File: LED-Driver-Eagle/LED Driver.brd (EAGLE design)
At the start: 21.3 x 25.4 mm, 10 parts, among them U3 LM4041A12DBZ

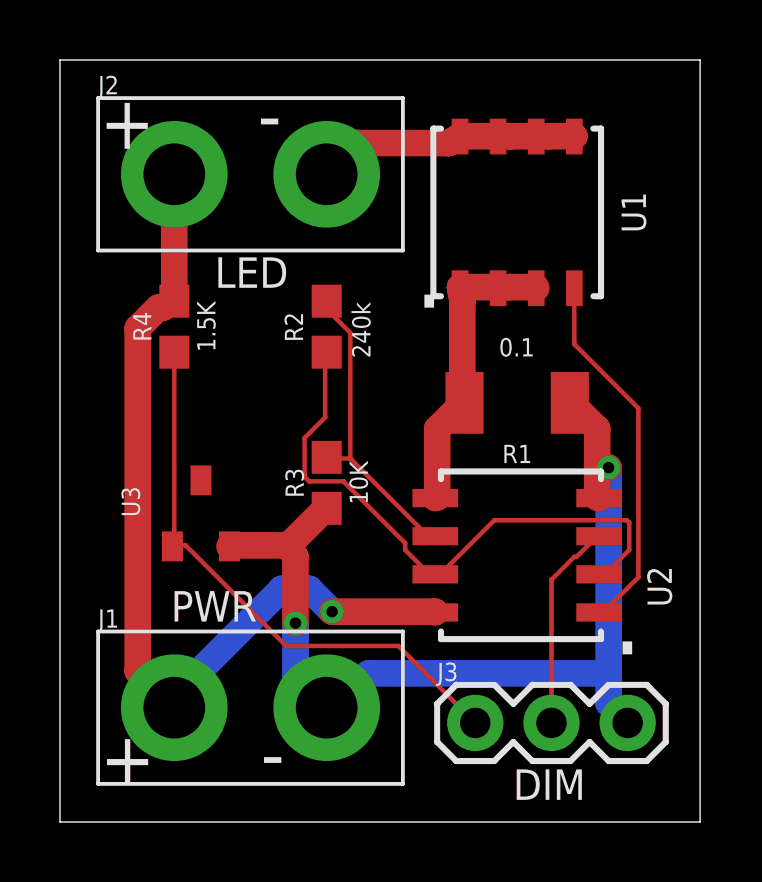
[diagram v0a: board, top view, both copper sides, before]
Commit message: Changed U1 and U2 to MF and OA
Updated Gerbers and eagle board files
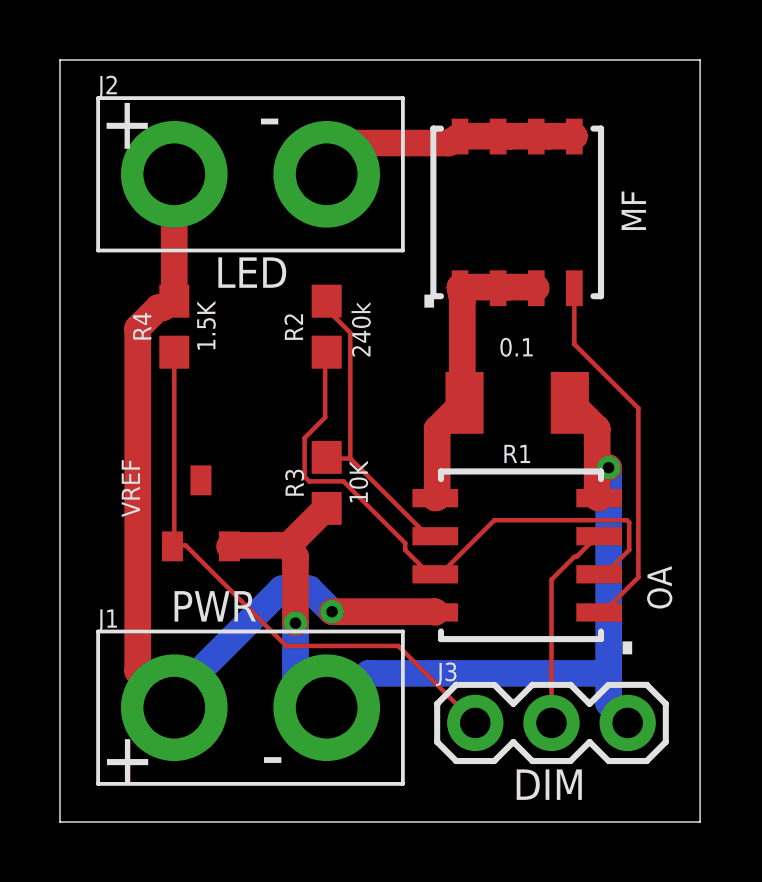
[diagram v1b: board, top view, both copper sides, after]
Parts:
- renumbered U$1 to M$F, U$2 to O$A
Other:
- board text added: "MF"
- board text added: "OA"
- board text added: "VREF"
- board text removed: "U1"
- board text removed: "U2"
- board text removed: "U3"
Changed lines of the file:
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@@
 <drawing>
 <settings>
-<setting alwaysvectorfont="yes"/>
+<setting alwaysvectorfont="no"/>
 <setting verticaltext="up"/>
 </settings>
 <grid distance="0.5" unitdist="mil" unit="mil" style="lines" multiple="1" display="yes" altdistance="5" altunitdist="mil" altunit="mil"/>
 <layers>
-<layer number="1" name="Top" color="4" fill="1" visible="no" active="yes"/>
+<layer number="1" name="Top" color="4" fill="1" visible="yes" active="yes"/>
 <layer number="2" name="Route2" color="1" fill="3" visible="no" active="no"/>
 <layer number="3" name="Route3" color="4" fill="3" visible="no" active="no"/>
@@
 <layer number="19" name="Unrouted" color="6" fill="1" visible="yes" active="yes"/>
 <layer number="20" name="Dimension" color="24" fill="1" visible="yes" active="yes"/>
-<layer number="21" name="tPlace" color="7" fill="1" visible="no" active="yes"/>
+<layer number="21" name="tPlace" color="7" fill="1" visible="yes" active="yes"/>
 <layer number="22" name="bPlace" color="7" fill="1" visible="yes" active="yes"/>
-<layer number="23" name="tOrigins" color="15" fill="1" visible="no" active="yes"/>
+<layer number="23" name="tOrigins" color="15" fill="1" visible="yes" active="yes"/>
 <layer number="24" name="bOrigins" color="15" fill="1" visible="yes" active="yes"/>
-<layer number="25" name="tNames" color="7" fill="1" visible="no" active="yes"/>
+<layer number="25" name="tNames" color="7" fill="1" visible="yes" active="yes"/>
 <layer number="26" name="bNames" color="7" fill="1" visible="yes" active="yes"/>
-<layer number="27" name="tValues" color="7" fill="1" visible="no" active="yes"/>
-<layer number="28" name="bValues" color="7" fill="1" visible="no" active="yes"/>
+<layer number="27" name="tValues" color="7" fill="1" visible="yes" active="yes"/>
+<layer number="28" name="bValues" color="7" fill="1" visible="yes" active="yes"/>
 <layer number="29" name="tStop" color="7" fill="3" visible="no" active="yes"/>
 <layer number="30" name="bStop" color="7" fill="6" visible="no" active="yes"/>
@@
 <layer number="37" name="tTest" color="7" fill="1" visible="no" active="yes"/>
 <layer number="38" name="bTest" color="7" fill="1" visible="no" active="yes"/>
-<layer number="39" name="tKeepout" color="4" fill="11" visible="no" active="yes"/>
+<layer number="39" name="tKeepout" color="4" fill="11" visible="yes" active="yes"/>
 <layer number="40" name="bKeepout" color="1" fill="11" visible="yes" active="yes"/>
-<layer number="41" name="tRestrict" color="4" fill="10" visible="no" active="yes"/>
+<layer number="41" name="tRestrict" color="4" fill="10" visible="yes" active="yes"/>
 <layer number="42" name="bRestrict" color="1" fill="10" visible="yes" active="yes"/>
 <layer number="43" name="vRestrict" color="2" fill="10" visible="no" active="yes"/>
-<layer number="44" name="Drills" color="7" fill="1" visible="no" active="yes"/>
+<layer number="44" name="Drills" color="7" fill="1" visible="yes" active="yes"/>
 <layer number="45" name="Holes" color="7" fill="1" visible="yes" active="yes"/>
 <layer number="46" name="Milling" color="3" fill="1" visible="no" active="yes"/>
@@
 <layer number="49" name="Reference" color="7" fill="1" visible="no" active="yes"/>
 <layer number="50" name="dxf" color="7" fill="1" visible="no" active="no"/>
-<layer number="51" name="tDocu" color="7" fill="1" visible="no" active="yes"/>
+<layer number="51" name="tDocu" color="7" fill="1" visible="yes" active="yes"/>
 <layer number="52" name="bDocu" color="7" fill="1" visible="yes" active="yes"/>
 <layer number="53" name="tGND_GNDA" color="7" fill="9" visible="no" active="no"/>
@@
 </layers>
 <board>
-<fusionsync huburn="a.cGVyc29uYWw6dWUyYjA2ZTQw" projecturn="a.cGVyc29uYWw6dWUyYjA2ZTQwIzIwMTgwMjIzMTE5NDc3OTU2" f3durn="urn:adsk.wipprod:dm.lineage:CXPcsSRXTwSbw_zEyj-MFA" pcbguid="f8d63bc8-81ed-4c37-9df4-4ae1279349d0" lastpulledtime="" lastsyncedchangeguid="bf620849-5e47-bcb0-3e1e-9827651a09dc"/>
+<fusionsync huburn="a.cGVyc29uYWw6dWUyYjA2ZTQw" projecturn="a.cGVyc29uYWw6dWUyYjA2ZTQwIzIwMTgwMjIzMTE5NDc3OTU2" f3durn="urn:adsk.wipprod:dm.lineage:CXPcsSRXTwSbw_zEyj-MFA" pcbguid="f8d63bc8-81ed-4c37-9df4-4ae1279349d0" lastpulledtime="" lastsyncedchangeguid="f8490a45-2c41-1a33-4372-efb22b674da7"/>
 <plain>
 <wire x1="0" y1="0" x2="21.336" y2="0" width="0" layer="20"/>
@@
 <vertex x="13.5001" y="11.0363"/>
 </polygon>
-<text x="19.5326" y="19.6342" size="0.8128" layer="25" rot="R90">U1</text>
-<text x="19.5834" y="8.5344" size="0.8128" layer="25" rot="R270">U2</text>
+<text x="19.5326" y="19.6342" size="0.8128" layer="25" rot="R90">MF</text>
+<text x="19.5834" y="8.5344" size="0.8128" layer="25" rot="R270">OA</text>
 <polygon width="0.002540625" layer="52">
 <vertex x="14.8209" y="14.3383"/>
@@
 <text x="15.1003" y="0.7366" size="1.016" layer="25">DIM</text>
 <text x="5.1562" y="17.8054" size="1.016" layer="25">LED</text>
-<text x="2.667" y="10.16" size="0.6096" layer="25" font="vector" ratio="20" rot="R90">U3</text>
+<text x="2.667" y="10.16" size="0.6096" layer="25" font="vector" ratio="20" rot="R90">VREF</text>
 <text x="12.9667" y="16.2941" size="1.778" layer="22" rot="MR270">CECFC</text>
 </plain>
@@
 <attribute name="VALUE" x="4.572" y="16.51" size="0.6096" layer="25" font="vector" ratio="20" rot="R90" align="top-center"/>
 </element>
-<element name="U$1" library="CECFC" package="SO8" value="SI4712DY" x="15.24" y="20.32" smashed="yes" rot="R90"/>
-<element name="U$2" library="CECFC" package="SOIC8" value="MC33202DR2G" x="15.24" y="8.89" smashed="yes" rot="R90"/>
+<element name="M$F" library="CECFC" package="SO8" value="SI4712DY" x="15.24" y="20.32" smashed="yes" rot="R90"/>
+<element name="O$A" library="CECFC" package="SOIC8" value="MC33202DR2G" x="15.24" y="8.89" smashed="yes" rot="R90"/>
 </elements>
 <signals>
 <signal name="VCC" class="1">
 <contactref element="R4" pad="2"/>
-<contactref element="U$2" pad="8"/>
+<contactref element="O$A" pad="8"/>
 <contactref element="J1" pad="1"/>
 <contactref element="J2" pad="1"/>
@@
 <contactref element="U3" pad="2"/>
 <contactref element="R1" pad="1"/>
-<contactref element="U$2" pad="4"/>
+<contactref element="O$A" pad="4"/>
 <contactref element="J1" pad="2"/>
 <contactref element="R3" pad="1"/>
@@
 </signal>
 <signal name="N$2">
-<contactref element="U$2" pad="3"/>
+<contactref element="O$A" pad="3"/>
 <contactref element="J3" pad="2"/>
 <wire x1="17.2212" y1="8.8392" x2="17.907" y2="9.525" width="0.1524" layer="1"/>
@@
 </signal>
 <signal name="N$3">
-<contactref element="U$2" pad="1"/>
-<contactref element="U$1" pad="4"/>
+<contactref element="O$A" pad="1"/>
+<contactref element="M$F" pad="4"/>
 <wire x1="17.145" y1="15.9258" x2="17.145" y2="17.7927" width="0.1524" layer="1"/>
 <wire x1="19.2786" y1="13.7922" x2="17.145" y2="15.9258" width="0.1524" layer="1"/>
@@
 </signal>
 <signal name="N$4" class="1">
-<contactref element="U$1" pad="5"/>
-<contactref element="U$1" pad="6"/>
-<contactref element="U$1" pad="7"/>
-<contactref element="U$1" pad="8"/>
+<contactref element="M$F" pad="5"/>
+<contactref element="M$F" pad="6"/>
+<contactref element="M$F" pad="7"/>
+<contactref element="M$F" pad="8"/>
 <contactref element="J2" pad="2"/>
 <wire x1="14.5542" y1="22.86" x2="13.335" y2="22.86" width="0.889" layer="1"/>
@@
 </signal>
 <signal name="N$5" class="1">
-<contactref element="U$1" pad="1"/>
-<contactref element="U$1" pad="2"/>
-<contactref element="U$1" pad="3"/>
+<contactref element="M$F" pad="1"/>
+<contactref element="M$F" pad="2"/>
+<contactref element="M$F" pad="3"/>
 <contactref element="R1" pad="2"/>
-<contactref element="U$2" pad="5"/>
+<contactref element="O$A" pad="5"/>
 <wire x1="14.5542" y1="17.8308" x2="13.335" y2="17.8308" width="0.889" layer="1"/>
 <wire x1="13.335" y1="17.8308" x2="13.335" y2="17.7927" width="0.889" layer="1"/>
@@
 </signal>
 <signal name="N$6">
-<contactref element="U$2" pad="7"/>
+<contactref element="O$A" pad="7"/>
 <contactref element="R2" pad="2"/>
-<contactref element="U$2" pad="2"/>
+<contactref element="O$A" pad="2"/>
 <wire x1="8.8392" y1="13.4874" x2="8.8392" y2="15.621" width="0.1524" layer="1"/>
 <wire x1="8.1534" y1="12.8016" x2="8.8392" y2="13.4874" width="0.1524" layer="1"/>
@@
 <contactref element="R2" pad="1"/>
 <contactref element="R3" pad="2"/>
-<contactref element="U$2" pad="6"/>
+<contactref element="O$A" pad="6"/>
 <wire x1="9.6774" y1="12.1158" x2="8.9154" y2="12.1158" width="0.1524" layer="1"/>
 <wire x1="12.2682" y1="9.525" x2="9.6774" y2="12.1158" width="0.1524" layer="1"/>
